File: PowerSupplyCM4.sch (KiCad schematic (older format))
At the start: 60 parts, among them J7 BAT, J8 IGNITION, Q1 NVMFS5C442NL, Q2 SQ2362ES-T1_GE3, Q3 SQD50P06-15L_GE3, Q4 SQJ461EP-T1-GE3, U10 VOMA617A, U11 VOMA617A, U12 LM53635LQRNL*Q1, U13 TLVH431AQDBVRQ1, U14 LM74610-Q1

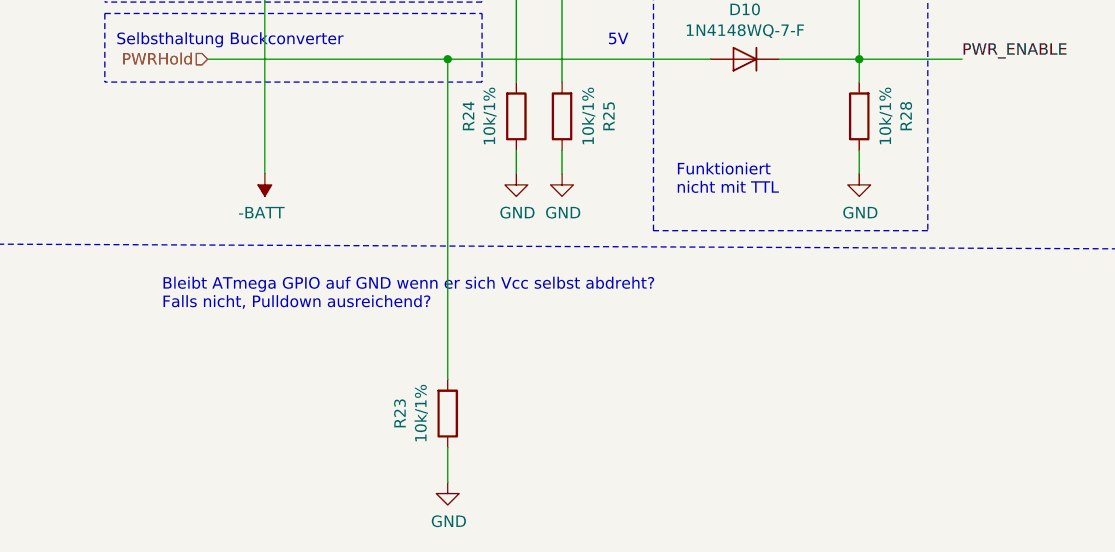
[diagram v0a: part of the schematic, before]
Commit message: [mod:] Atmega issues resolved: Programming interface, self cutoff
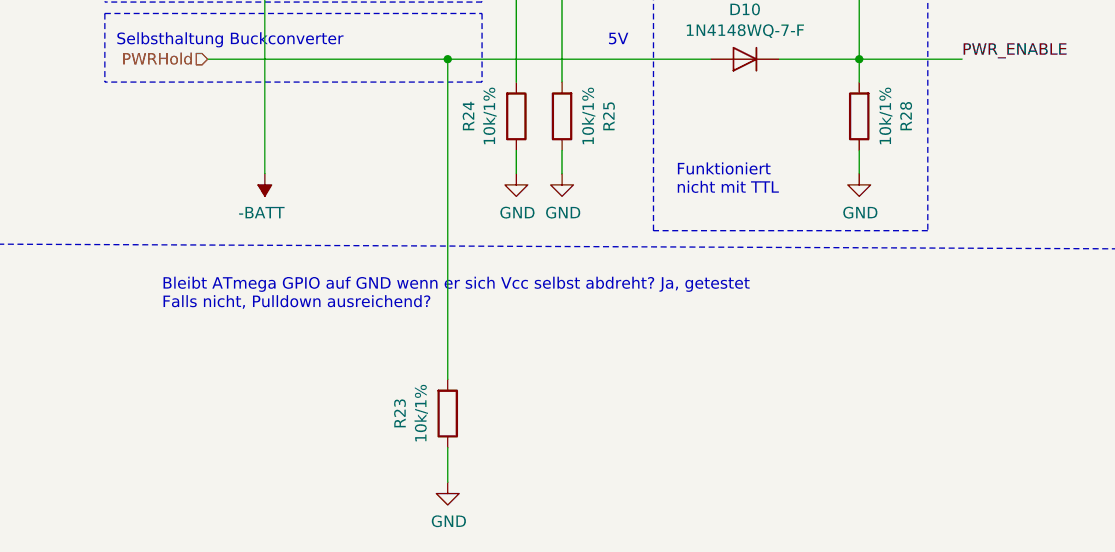
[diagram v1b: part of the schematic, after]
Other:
- note added: "Bleibt ATmega GPIO auf GND wenn er sich Vcc selbst abdreht? Ja, getestet\nFalls nicht, Pulldown ausreichend?"
- note removed: "Bleibt ATmega GPIO auf GND wenn er sich Vcc selbst abdreht?\nFalls nicht, Pulldown ausreichend?"
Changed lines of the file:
@@
 Selbsthaltung Buckconverter
 Text Notes 4800 14550 0    50   ~ 0
-Bleibt ATmega GPIO auf GND wenn er sich Vcc selbst abdreht?\nFalls nicht, Pulldown ausreichend?
+Bleibt ATmega GPIO auf GND wenn er sich Vcc selbst abdreht? Ja, getestet\nFalls nicht, Pulldown ausreichend?
 $Comp
 L Device:R R23

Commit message: - Anpassungen ToDos und kleinere Änderungen
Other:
- note removed: "Bleibt ATmega GPIO auf GND wenn er sich Vcc selbst abdreht? Ja, getestet\nFalls nicht, Pulldown ausreichend?"
- note removed: "Funktioniert \nnicht mit TTL"
- moved on the sheet: R23
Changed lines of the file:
@@
 	7850 13450 7850 13550
 Wire Wire Line
-	5000 13450 6050 13450
+	5000 13450 5950 13450
 Wire Wire Line
 	7850 13850 7850 13950
@@
 	7500 13450 7850 13450
 Text Notes 9100 13800 0    50   ~ 0
-Ermöglicht verzögertes Abschalten durch ATMEGA\n\nAus DS LM53635 S. 16:\nStart-up and shutdown of the LM53625/35-Q1 are controlled by the EN input. \nApplying a voltage of ≥ 2 V activates the device, while a voltage of ≤ 0.8 V is required to shut it down. \n(Max EN voltage: 40V (wie VIN))\nD.h. ATmega Ausgangspegel von 5V reicht für die Ansteuerung\nDas Zündungsignal muss aber auf 12V bleiben, da 5V nur verfügbar wenn alles an ist.\n\nÄnderungen:\n- Topologie geändert: OCs nun parallel an Ignition, statt in Reihe\n- ODER Schaltung um 2te Diode und Pulldown ergänzt\n- PWR_Enable an Buckconverter angeschlossen\n- Optokoppler für ATmega Ausgangssignal entfernt, da galv. Trennung hier unnötig\n- SMD Optokoppler\n- Nicht Invertierender Ausgang\n- Eingangsschutzbeschaltung wie bei Vbat\n\nBerechnung Vorwiderstand OC:\nLED Vf  1,33 - 1,5 V @ 5mA (max 20mA)\nKFZ Spannung max ~14V\n=> R = (14V -1,4V) / 5mA = 2500\nWahl: 2k2, etwas mehr Strom, genug Sicherheit\n\n
+Ermöglicht verzögertes Abschalten durch ATMEGA\n\nAus DS LM53635 S. 16:\nStart-up and shutdown of the LM53625/35-Q1 are controlled by the EN input. \nApplying a voltage of ≥ 2 V activates the device, while a voltage of ≤ 0.8 V is required to shut it down. \n(Max EN voltage: 40V (wie VIN))\nD.h. ATmega Ausgangspegel von 5V reicht für die Ansteuerung\nDas Zündungsignal muss aber auf 12V bleiben, da 5V nur verfügbar wenn alles an ist.\n\nÄnderungen:\n- Topologie geändert: OCs nun parallel an Ignition, statt in Reihe\n- ODER Schaltung um 2te Diode und Pulldown ergänzt (nicht fuer TTL)\n- PWR_Enable an Buckconverter angeschlossen\n- Optokoppler für ATmega Ausgangssignal entfernt, da galv. Trennung hier unnötig\n- SMD Optokoppler\n- Nicht Invertierender Ausgang\n- Eingangsschutzbeschaltung wie bei Vbat\n\nBerechnung Vorwiderstand OC:\nLED Vf  1,33 - 1,5 V @ 5mA (max 20mA)\nKFZ Spannung max ~14V\n=> R = (14V -1,4V) / 5mA = 2500\nWahl: 2k2, etwas mehr Strom, genug Sicherheit\n\n
 Connection ~ 7850 13450
 Text Label 8300 13450 0    50   ~ 0
@@
 Text Notes 4600 13400 0    50   ~ 0
 Selbsthaltung Buckconverter
-Text Notes 4800 14550 0    50   ~ 0
-Bleibt ATmega GPIO auf GND wenn er sich Vcc selbst abdreht? Ja, getestet\nFalls nicht, Pulldown ausreichend?
 $Comp
 L Device:R R23
 U 1 1 616BB340
-P 6050 15000
-F 0 "R23" V 5843 15000 50  0000 C CNN
-F 1 "10k/1%" V 5934 15000 50  0000 C CNN
-F 2 "Resistor_SMD:R_0402_1005Metric" V 5980 15000 50  0001 C CNN
-F 3 "~" H 6050 15000 50  0001 C CNN
-	1    6050 15000
+P 5950 13700
+F 0 "R23" V 5743 13700 50  0000 C CNN
+F 1 "10k/1%" V 5834 13700 50  0000 C CNN
+F 2 "Resistor_SMD:R_0402_1005Metric" V 5880 13700 50  0001 C CNN
+F 3 "~" H 5950 13700 50  0001 C CNN
+	1    5950 13700
 	1    0    0    1
 $EndComp
@@
 L power:GND #PWR0146
 U 1 1 616BB34B
-P 6050 15300
-F 0 "#PWR0146" H 6050 15050 50  0001 C CNN
-F 1 "GND" H 6055 15127 50  0000 C CNN
-F 2 "" H 6050 15300 50  0001 C CNN
-F 3 "" H 6050 15300 50  0001 C CNN
-	1    6050 15300
+P 5950 13950
+F 0 "#PWR0146" H 5950 13700 50  0001 C CNN
+F 1 "GND" H 5955 13777 50  0000 C CNN
+F 2 "" H 5950 13950 50  0001 C CNN
+F 3 "" H 5950 13950 50  0001 C CNN
+	1    5950 13950
 	1    0    0    -1
 $EndComp
 Wire Wire Line
-	6050 15300 6050 15150
+	5950 13950 5950 13850
 Wire Wire Line
 	5950 13100 6350 13100
 Wire Wire Line
-	6050 13450 6050 14850
-Connection ~ 6050 13450
+	5950 13450 5950 13550
+Connection ~ 5950 13450
 Wire Wire Line
-	6050 13450 7200 13450
-Text Notes 7050 14050 0    50   ~ 0
-Funktioniert \nnicht mit TTL
+	5950 13450 7200 13450
 Wire Wire Line
 	2550 12750 2550 12550

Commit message: - Schaltbare BL Versorgung fertig - kleinere Value Anpassungen - Finale Annotation
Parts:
- removed J7: BAT, Connector_PinHeader_2.54mm:PinHeader_1x02_P2.54mm_Horizontal, symbol Connector_Generic:Conn_01x02
- removed J8: IGNITION, Connector_PinHeader_2.54mm:PinHeader_1x02_P2.54mm_Horizontal, symbol Connector_Generic:Conn_01x02
- removed Q4: SQJ461EP-T1-GE3, TeKaDe:PowerPAK-SO-8L-SINGLE, symbol TeKaDe:SQJ461EP-T1-GE3
- added J9: Conn_01x03, TerminalBlock_Phoenix:TerminalBlock_Phoenix_MKDS-1,5-3_1x03_P5.00mm_Horizontal, symbol Connector_Generic:Conn_01x03
- renumbered C56 to C10, C57 to C11, C58 to C12, C59 to C13, C60 to C14, C61 to C15, C62 to C16, C63 to C17, C64 to C18, C65 to C19, C66 to C20, C67 to C21, C68 to C22, C69 to C23, C70 to C24, C71 to C25, C72 to C26, C73 to C27, C74 to C28, C75 to C29, C76 to C30, C51 to C5, C52 to C6, C53 to C7, C54 to C8, C55 to C9, D5 to D1, D6 to D2, D7 to D3, D8 to D4, D9 to D5, D10 to D6, D11 to D7, L1 to L2, L2 to L3, Q1 to Q2, Q2 to Q3, Q3 to Q4, R20 to R17, R21 to R18, R22 to R19, R23 to R20, R24 to R21, R25 to R22, R26 to R23, R27 to R24, R28 to R25, R29 to R26, R30 to R27, R31 to R28, R32 to R29, U10 to U2, U11 to U3, U12 to U4, U13 to U5, U14 to U6
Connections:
- net +BATT: now also J9.1 (Pin_1)
- net -BATT: now also J9.2 (Pin_2)
- net IGNITION: now reaches C14.1, C8.1, D3.1 (K), R17.2, R18.2
- net IGNITION: now also J9.3 (Pin_3)

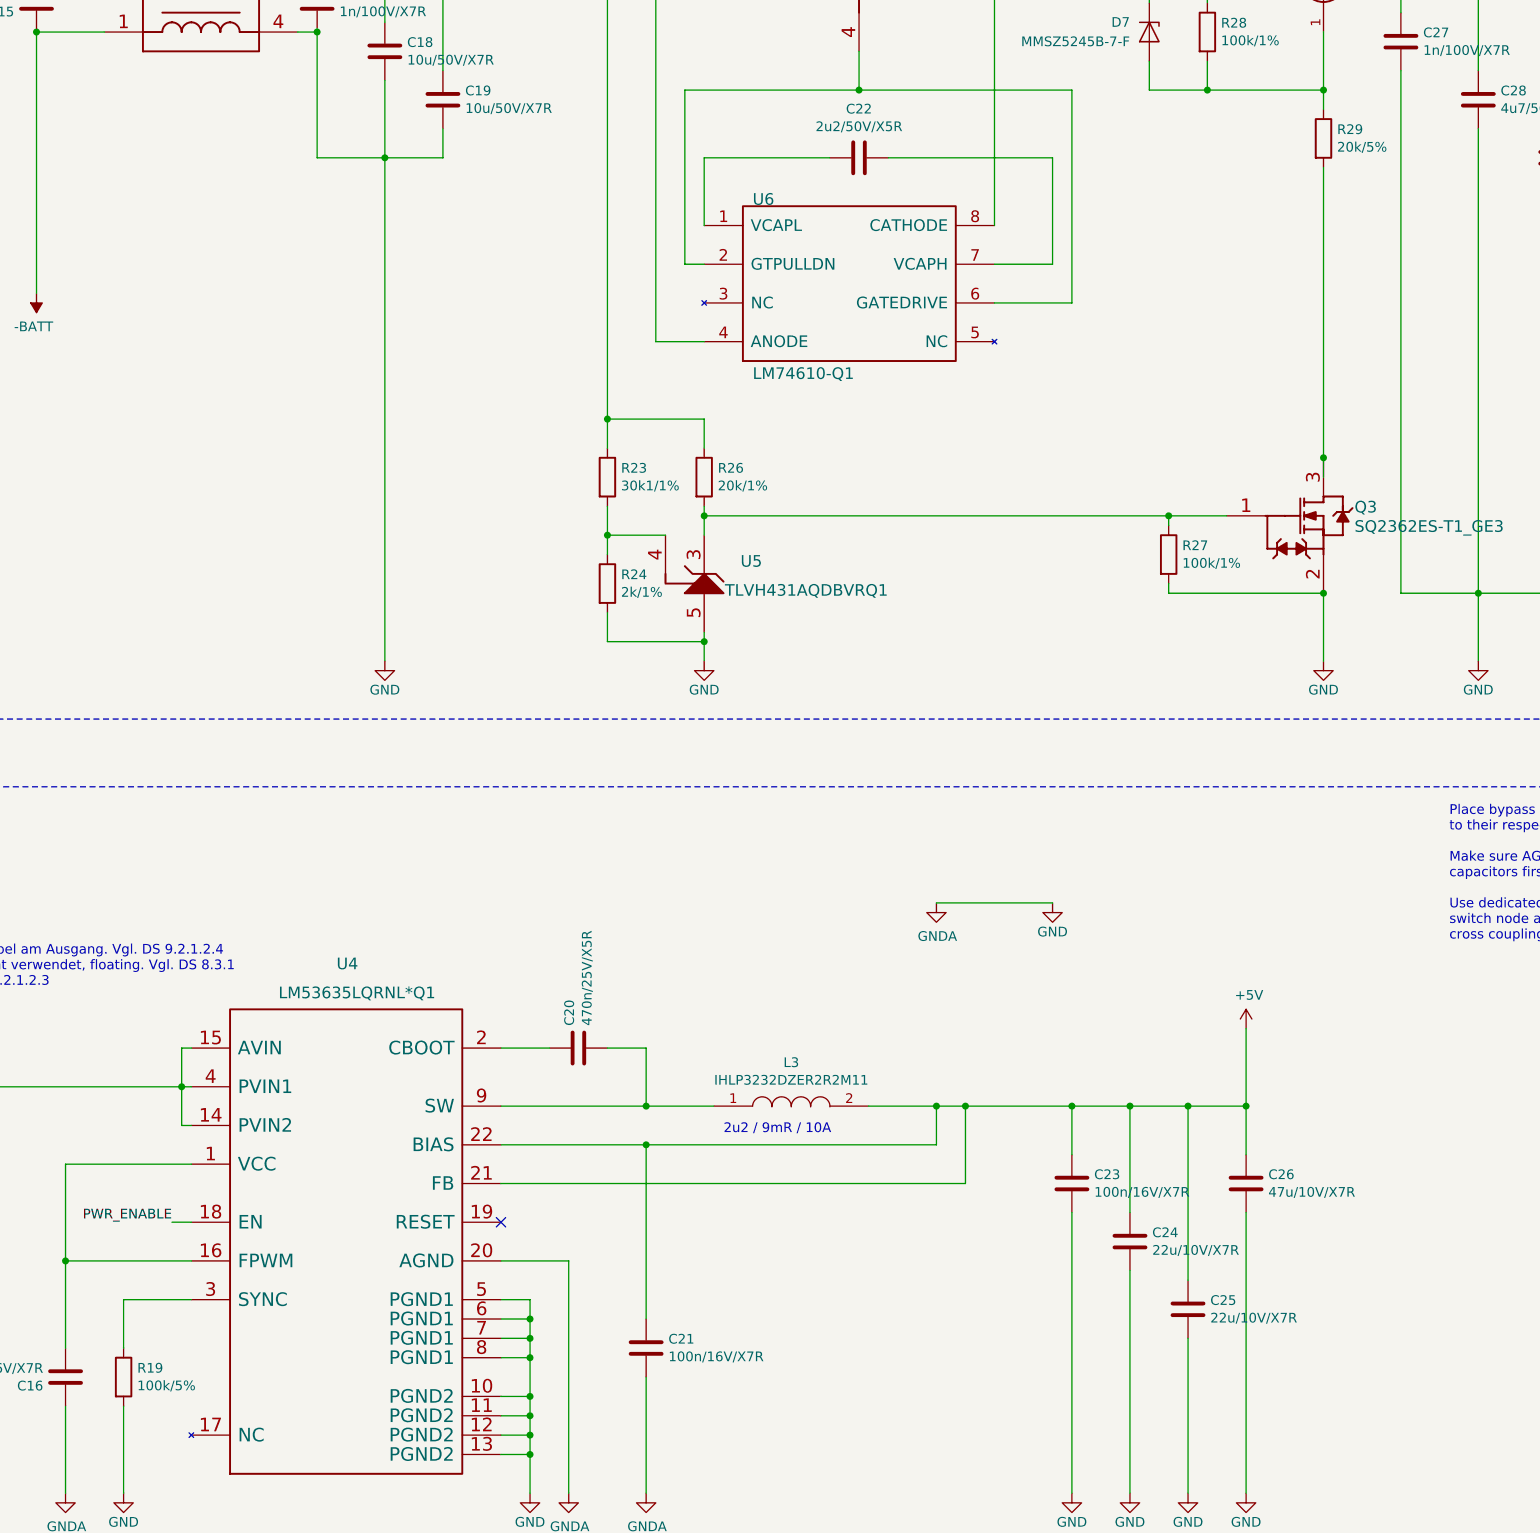
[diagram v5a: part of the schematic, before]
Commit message: - Bauteile konsolidiert
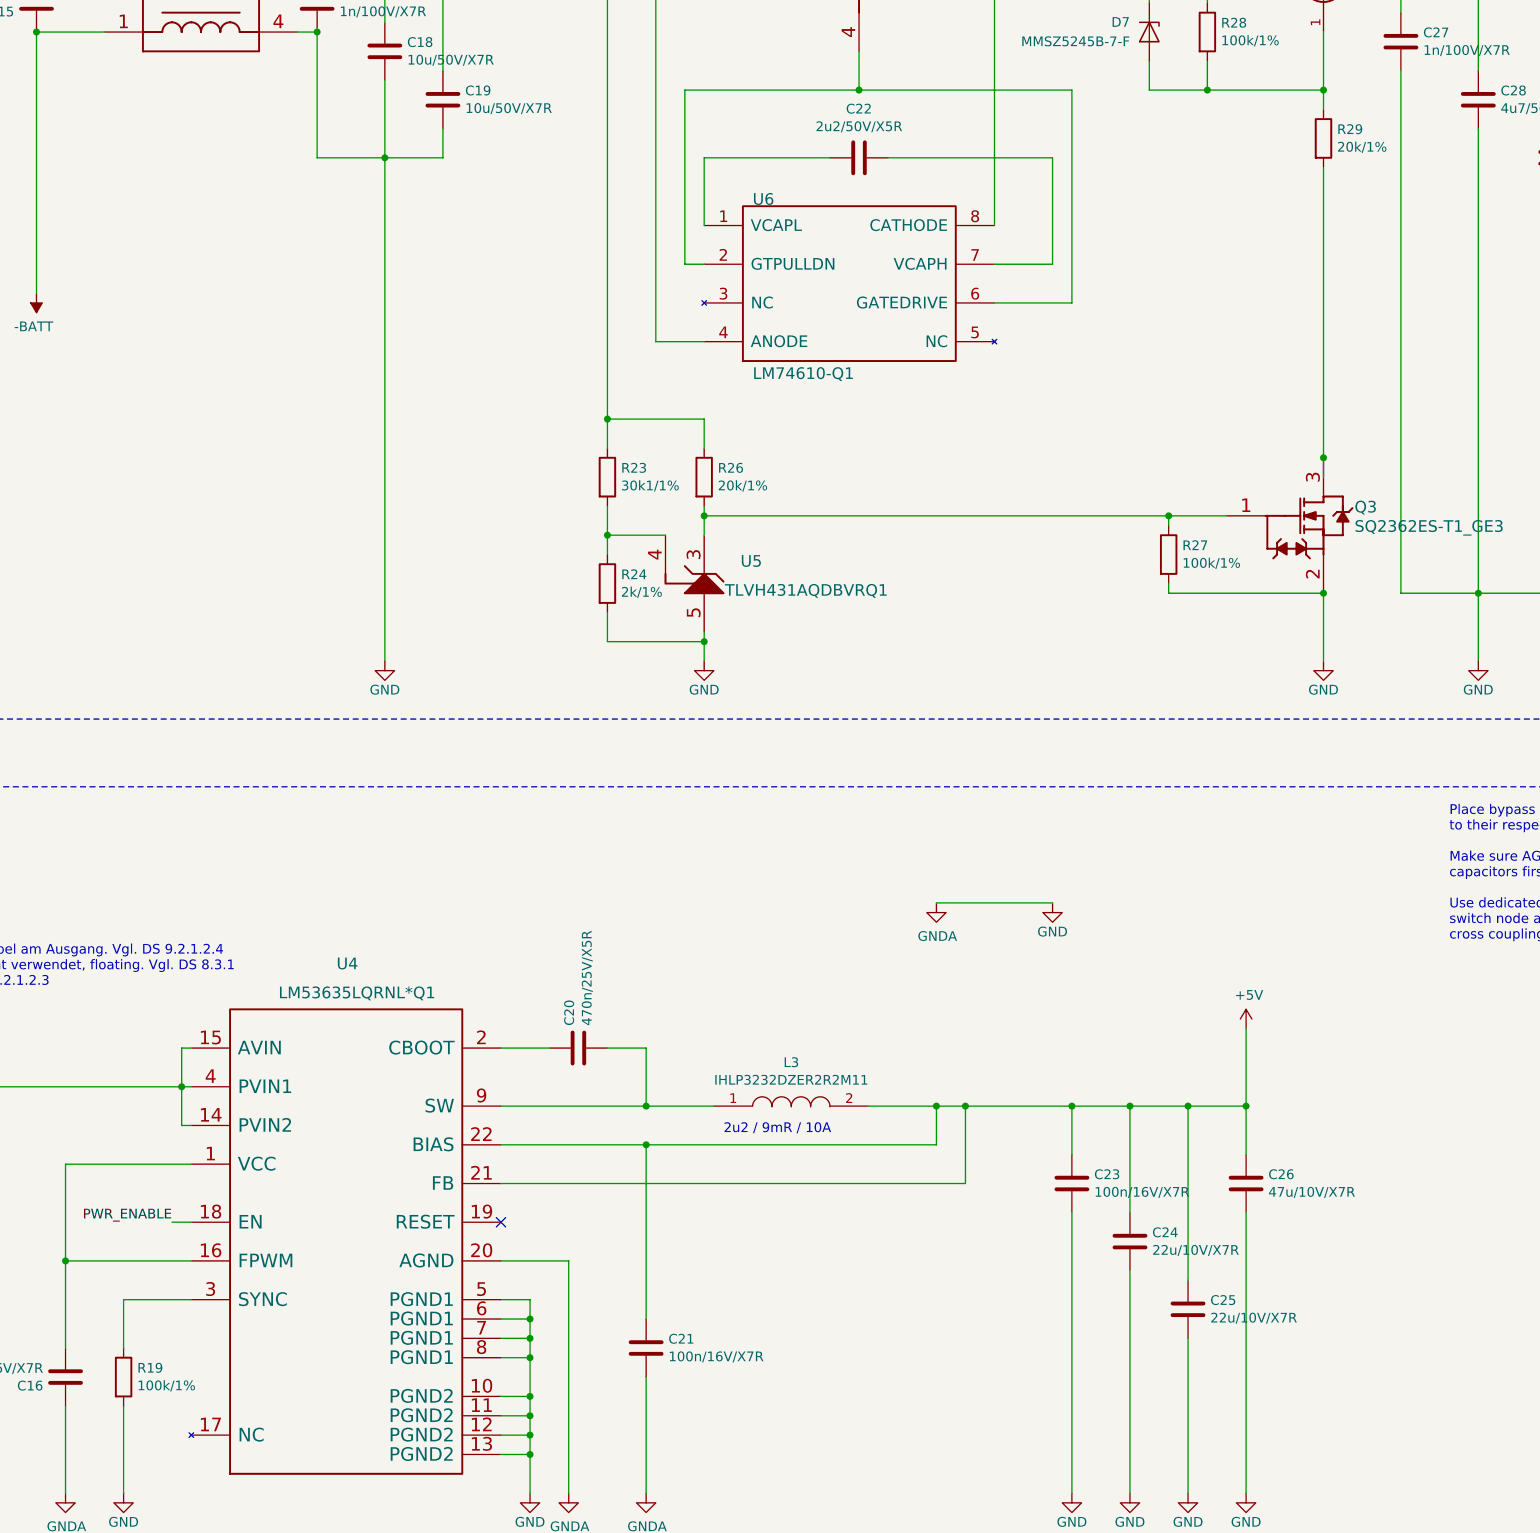
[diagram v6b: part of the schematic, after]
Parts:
- R19: value 100k/5% -> 100k/1%
- R29: value 20k/5% -> 20k/1%
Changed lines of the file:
@@
 P 5300 9750
 F 0 "R19" H 5370 9796 50  0000 L CNN
-F 1 "100k/5%" H 5370 9705 50  0000 L CNN
+F 1 "100k/1%" H 5370 9705 50  0000 L CNN
 F 2 "Resistor_SMD:R_0402_1005Metric" V 5230 9750 50  0001 C CNN
 F 3 "~" H 5300 9750 50  0001 C CNN
@@
 P 11500 3350
 F 0 "R29" H 11570 3396 50  0000 L CNN
-F 1 "20k/5%" H 11570 3305 50  0000 L CNN
+F 1 "20k/1%" H 11570 3305 50  0000 L CNN
 F 2 "Resistor_SMD:R_0402_1005Metric" V 11430 3350 50  0001 C CNN
 F 3 "~" H 11500 3350 50  0001 C CNN

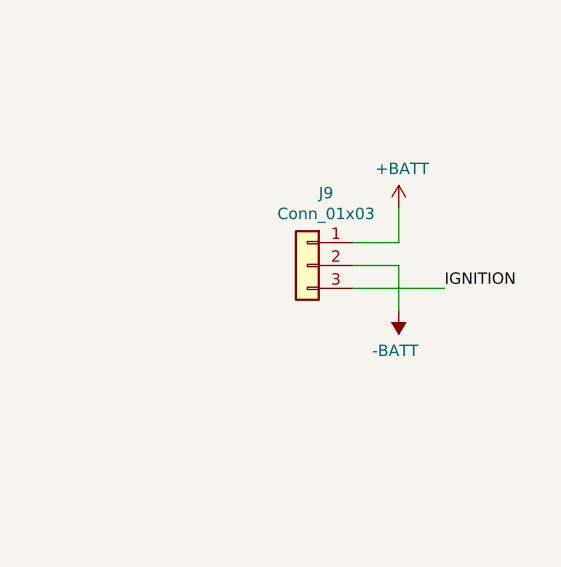
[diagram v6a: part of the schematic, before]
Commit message: - neue Stecker hinzugefügt, Annotation überall entsprechend angepasst Footprint fehlt noch
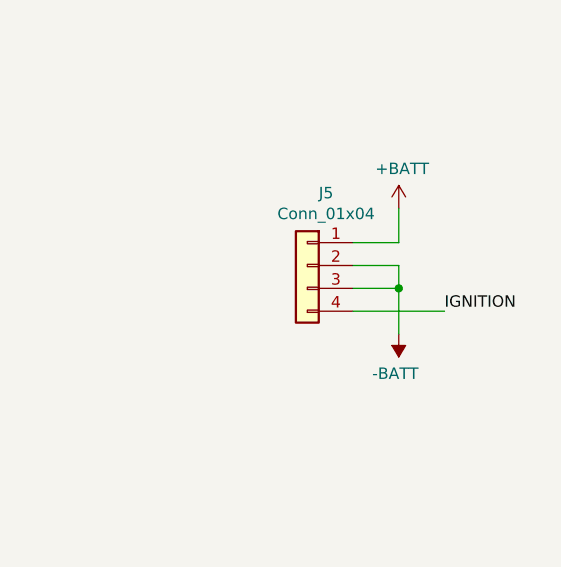
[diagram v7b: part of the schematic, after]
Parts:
- removed J9: Conn_01x03, TerminalBlock_Phoenix:TerminalBlock_Phoenix_MKDS-1,5-3_1x03_P5.00mm_Horizontal, symbol Connector_Generic:Conn_01x03
- added J5: Conn_01x04, Connector_PinSocket_2.54mm:PinSocket_1x04_P2.54mm_Vertical, symbol Connector_Generic:Conn_01x04
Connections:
- net +BATT: now also J5.1 (Pin_1)
- net -BATT: now also J5.2 (Pin_2), J5.3 (Pin_3)
- net IGNITION: now also J5.4 (Pin_4)
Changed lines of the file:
@@
 L power:-BATT #PWR063
 U 1 1 618BBB9B
-P 20100 3650
-F 0 "#PWR063" H 20100 3500 50  0001 C CNN
-F 1 "-BATT" H 20115 3823 50  0000 C CNN
-F 2 "" H 20100 3650 50  0001 C CNN
-F 3 "" H 20100 3650 50  0001 C CNN
-	1    20100 3650
+P 20100 3750
+F 0 "#PWR063" H 20100 3600 50  0001 C CNN
+F 1 "-BATT" H 20115 3923 50  0000 C CNN
+F 2 "" H 20100 3750 50  0001 C CNN
+F 3 "" H 20100 3750 50  0001 C CNN
+	1    20100 3750
 	-1   0    0    1
 $EndComp
@@
 	19900 3450 20100 3450
 Wire Wire Line
-	20100 3450 20100 3650
+	20100 3450 20100 3550
 Wire Wire Line
 	19900 3350 20100 3350
@@
 	20100 3350 20100 3200
 Wire Wire Line
-	19900 3550 20300 3550
-Text Label 20300 3550 0    50   ~ 0
+	19900 3650 20300 3650
+Text Label 20300 3650 0    50   ~ 0
 IGNITION
 Text Label 2300 11850 2    50   ~ 0
 IGNITION
-$Comp
-L Connector_Generic:Conn_01x03 J9
-U 1 1 618B94EC
-P 19700 3450
-F 0 "J9" H 19618 3767 50  0000 C CNN
-F 1 "Conn_01x03" H 19618 3676 50  0000 C CNN
-F 2 "TerminalBlock_Phoenix:TerminalBlock_Phoenix_MKDS-1,5-3_1x03_P5.00mm_Horizontal" H 19700 3450 50  0001 C CNN
-F 3 "~" H 19700 3450 50  0001 C CNN
-	1    19700 3450
-	-1   0    0    -1
-$EndComp
 $Comp
 L Device:C C14
@@
 	1    0    0    -1
 $EndComp
+$Comp
+L Connector_Generic:Conn_01x04 J5
+U 1 1 61974629
+P 19700 3450
+F 0 "J5" H 19618 3767 50  0000 C CNN
+F 1 "Conn_01x04" H 19618 3676 50  0000 C CNN
+F 2 "Connector_PinSocket_2.54mm:PinSocket_1x04_P2.54mm_Vertical" H 19700 3450 50  0001 C CNN
+F 3 "~" H 19700 3450 50  0001 C CNN
+	1    19700 3450
+	-1   0    0    -1
+$EndComp
+Wire Wire Line
+	19900 3550 20100 3550
+Connection ~ 20100 3550
+Wire Wire Line
+	20100 3550 20100 3750
 $EndSCHEMATC

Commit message: - Footprints inkl. 3D model aller Steckverbinder fertig
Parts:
- J5: footprint Connector_PinSocket_2.54mm:PinSocket_1x04_P2.54mm_Vertical -> TeKaDe:Molex_31101-0040
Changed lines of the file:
@@
 F 0 "J5" H 19618 3767 50  0000 C CNN
 F 1 "Conn_01x04" H 19618 3676 50  0000 C CNN
-F 2 "Connector_PinSocket_2.54mm:PinSocket_1x04_P2.54mm_Vertical" H 19700 3450 50  0001 C CNN
+F 2 "TeKaDe:Molex_31101-0040" H 19700 3450 50  0001 C CNN
 F 3 "~" H 19700 3450 50  0001 C CNN
 	1    19700 3450
